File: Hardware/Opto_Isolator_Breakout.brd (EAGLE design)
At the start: 15.2 x 12.7 mm, 16 parts, among them Q1 NPN, Q2 NPN, U1 OPTO

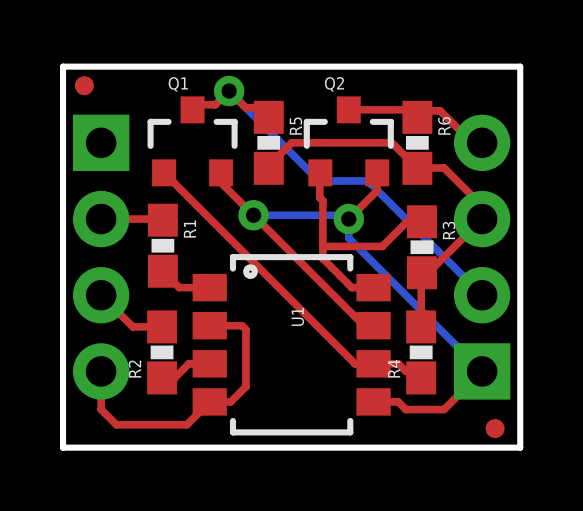
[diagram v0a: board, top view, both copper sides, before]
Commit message: Changed Res Values / SCH cleanup
changed r1 and r2 to 200K

Added version # and eng to board/sch files
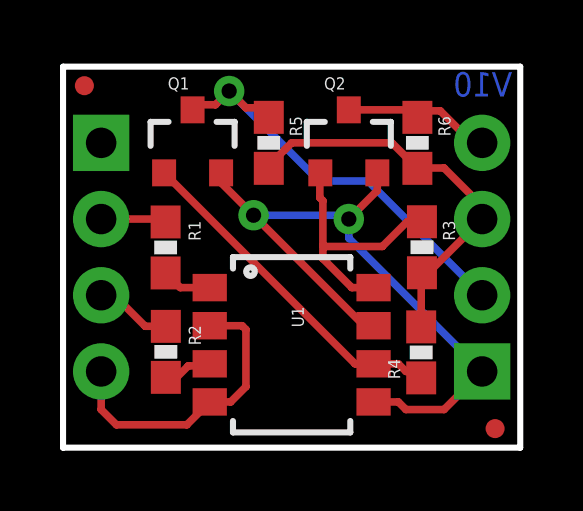
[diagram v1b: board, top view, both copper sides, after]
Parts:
- removed U$1: LOGO-SFESK, SparkFun:SFE-LOGO-FLAME
- added LOGO2: SFE_LOGO_FLAME.1_INCH, SparkFun-Aesthetics:SFE_LOGO_FLAME_.1
- R1, R2: value 220k -> 200k
- moved R2 0.13 mm to (3.43, 3.19), turned to 270 degrees
- moved R1 0.11 mm to (3.42, 6.67)
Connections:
- net IN2: now also R2.1; no longer R2.2
- net N$2: now also R2.2; no longer R2.1
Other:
- board text added: "N.Seidle"
- board text added: "Revised by: Patrick Alberts"
- board text added: "V10"
